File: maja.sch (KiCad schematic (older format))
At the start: 49 parts

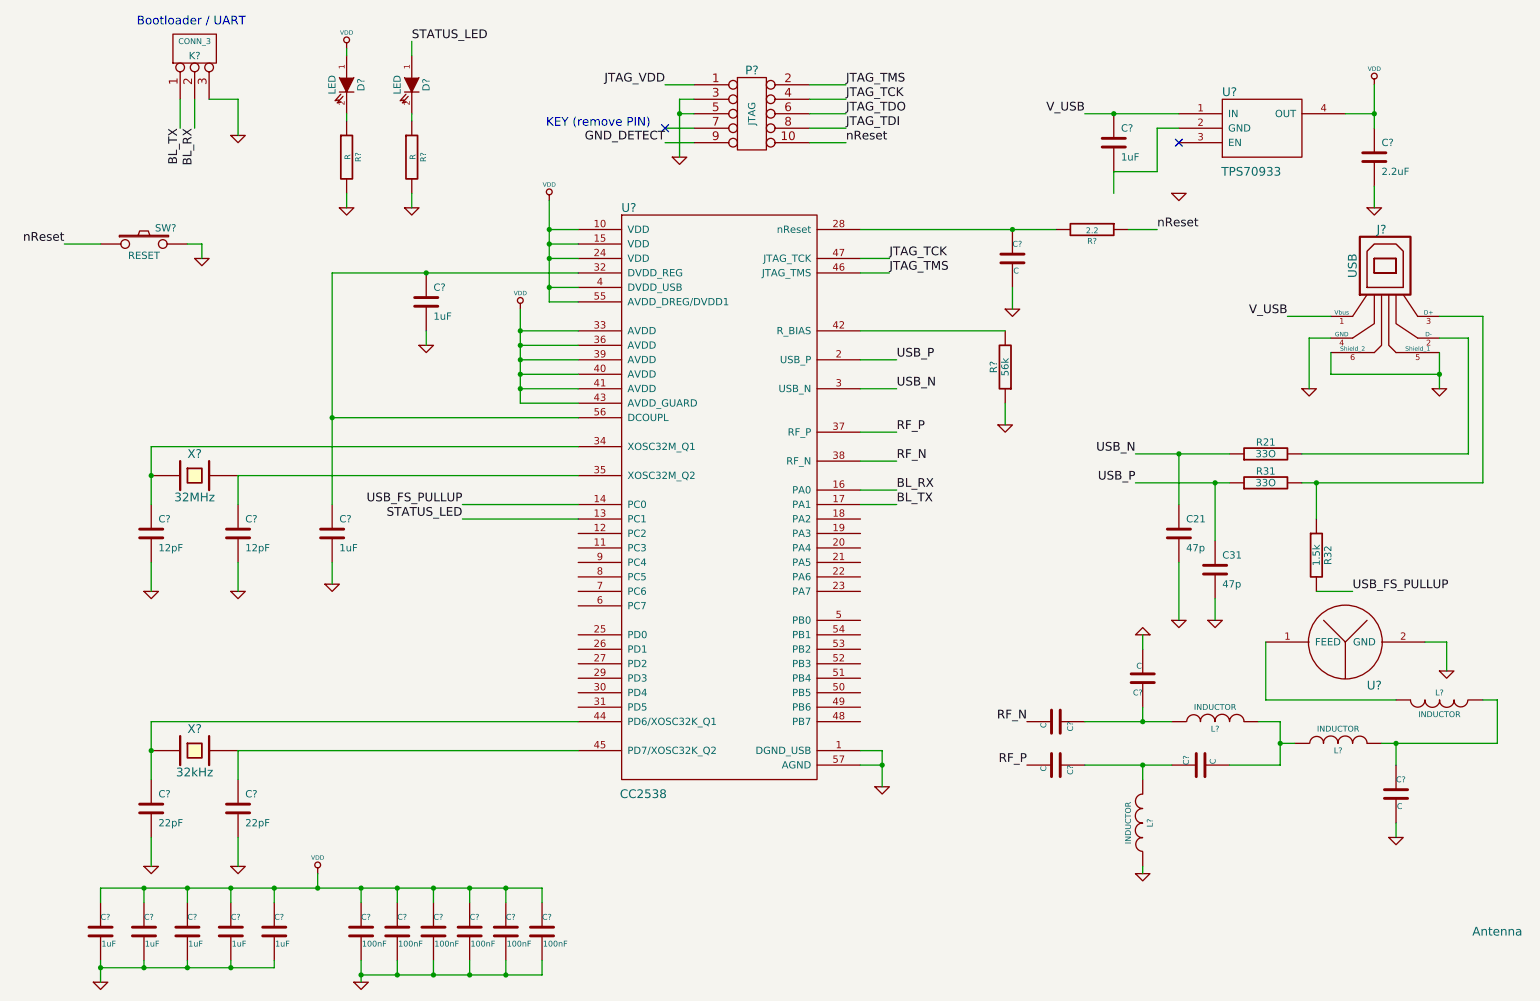
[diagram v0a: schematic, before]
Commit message: Started with basic PCB layout. Footprints must be checked again! I just choose one to be able to do a prelimary placement
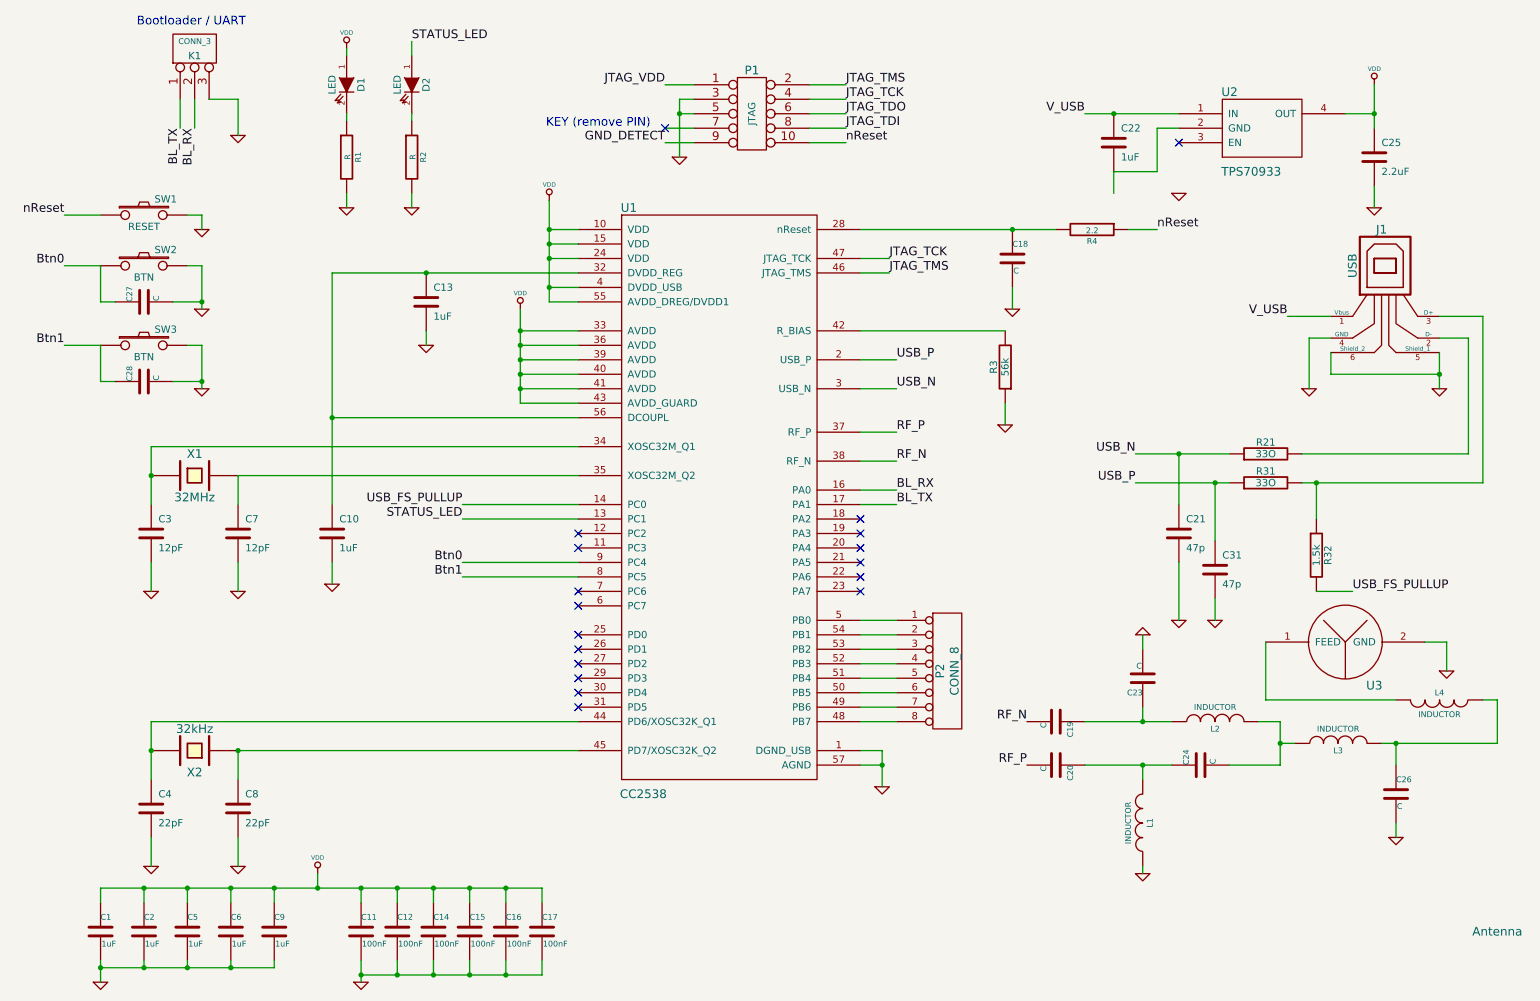
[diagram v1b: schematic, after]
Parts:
- added C27, C28: C, symbol C
- added P2: CONN_8, ~, symbol CONN_8
- added SW2, SW3: BTN, symbol SW_PUSH
- gave numbers to parts that had none: 44
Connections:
- net GND: now also C27.2, C28.2, SW2.2, SW3.2
- net at C4.1, U1.44 (PD6/XOSC32K_Q1): now also X2.2; no longer X2.1
- net at C8.1, U1.45 (PD7/XOSC32K_Q2): now also X2.1; no longer X2.2
- net at U1.48 (PB7): now also P2.8 (P8)
- net at U1.49 (PB6): now also P2.7 (P7)
- net at U1.5 (PB0): now also P2.1 (P1)
- net at U1.50 (PB5): now also P2.6 (P6)
- net at U1.51 (PB4): now also P2.5 (P5)
- net at U1.52 (PB3): now also P2.4 (P4)
- net at U1.53 (PB2): now also P2.3 (P3)
- net at U1.54 (PB1): now also P2.2 (P2)
- net Btn1: now reaches U1.8 (PC5)
- net Btn1: now also C28.1, SW3.1
- net Btn0: now reaches U1.9 (PC4)
- net Btn0: now also C27.1, SW2.1
- no-connect marks 2 -> 18
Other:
- moved on the sheet: SW1

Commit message: Started with routing, added two missing JTAG signals and corrected one library error
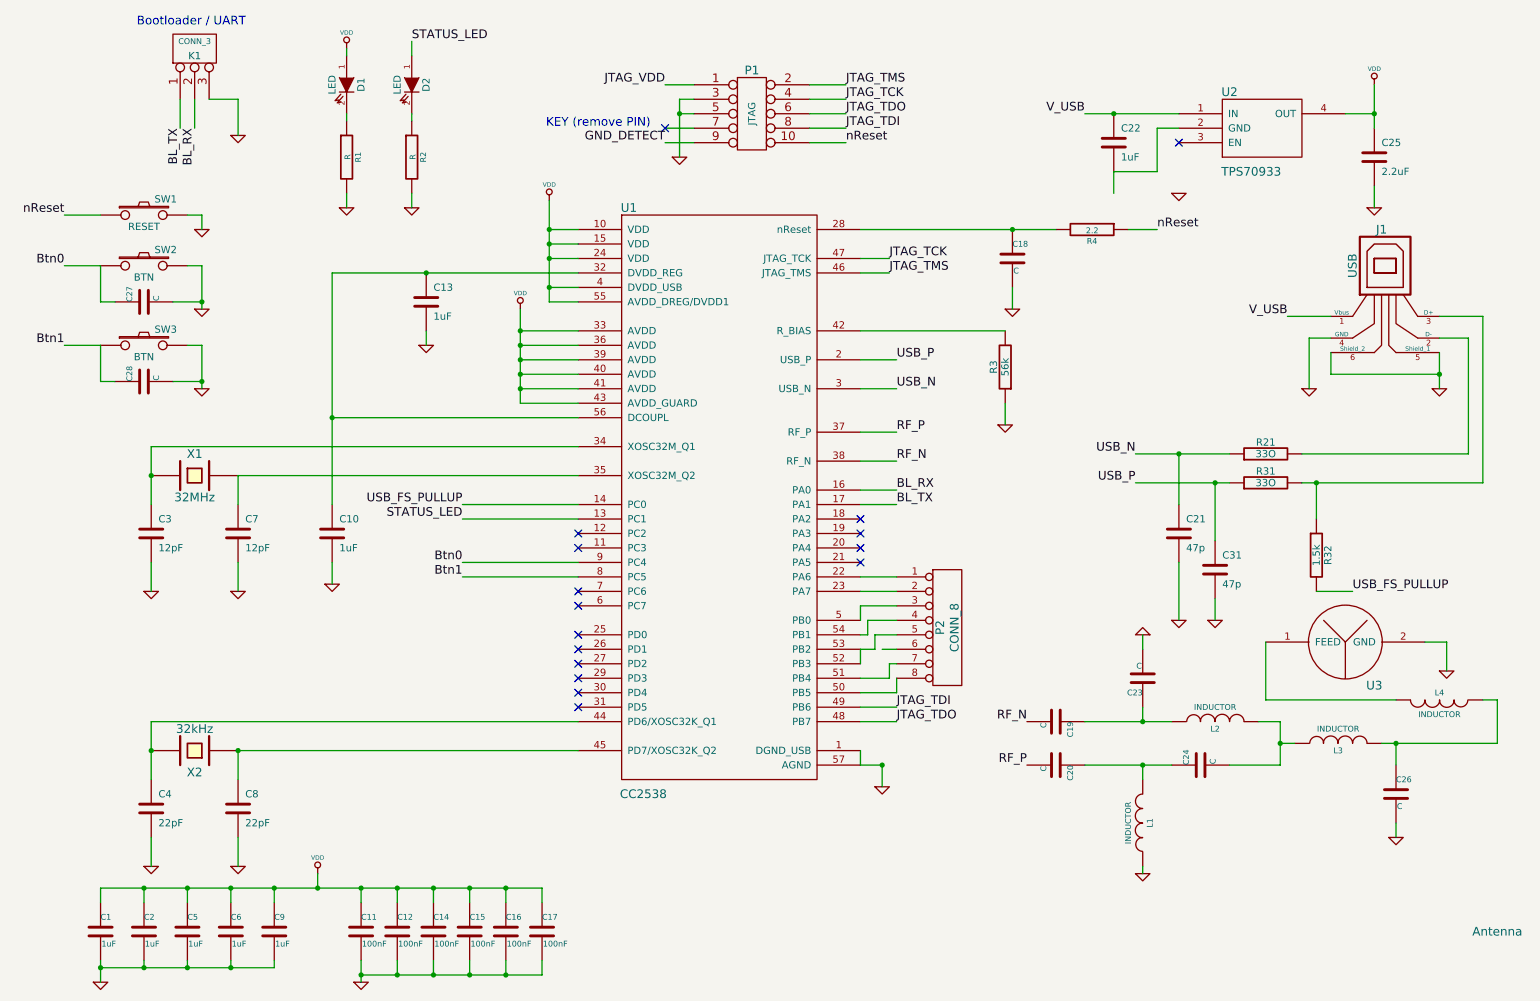
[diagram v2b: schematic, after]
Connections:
- net JTAG_TDI: now also U1.49 (PB6)
- net JTAG_TDO: now also U1.48 (PB7)
- net at U1.22 (PA6): now also P2.1 (P1)
- net at U1.23 (PA7): now also P2.2 (P2)
- net at P2.8 (P8): now also U1.50 (PB5); no longer U1.48 (PB7)
- net at P2.7 (P7): now also U1.51 (PB4); no longer U1.49 (PB6)
- net at U1.5 (PB0): now also P2.3 (P3); no longer P2.1 (P1)
- net at P2.6 (P6): no longer U1.50 (PB5)
- net at P2.5 (P5): now also U1.52 (PB3), U1.53 (PB2); no longer U1.51 (PB4)
- net at P2.4 (P4): now also U1.54 (PB1); no longer U1.52 (PB3)
- no-connect marks 18 -> 16
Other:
- moved on the sheet: P2
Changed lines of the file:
@@
 	0    -1   -1   0
-$EndComp
-$Comp
-L CC2538 U1
-U 1 1 531346AC
-P 5950 4950
-F 0 "U1" H 5050 8050 60  0000 C CNN
-F 1 "CC2538" H 5150 4000 60  0000 C CNN
-F 2 "" H 5950 4950 60  0001 C CNN
-F 3 "" H 5950 4950 60  0001 C CNN
-	1    5950 4950
-	1    0    0    -1
 $EndComp
 Text Label 1950 1300 3    60   ~ 0
@@
 	9750 2750 9900 2750
 Wire Wire Line
-	10650 2850 10650 3100
+	10650 2850 10650 3000
+Wire Wire Line
+	10650 3000 10650 3100
 Wire Wire Line
 	10650 2600 10950 2600
@@
 	10950 2600 10950 3750
 Wire Wire Line
-	10950 3750 9700 3750
+	10950 3750 9800 3750
+Wire Wire Line
+	9800 3750 9700 3750
 Wire Wire Line
 	4700 3900 3900 3900
@@
 	9100 4550 9100 4700
 Wire Wire Line
-	8550 3750 9200 3750
-Wire Wire Line
-	8550 3550 9200 3550
+	8550 3750 9100 3750
+Wire Wire Line
+	9100 3750 9200 3750
+Wire Wire Line
+	8550 3550 8850 3550
+Wire Wire Line
+	8850 3550 9200 3550
 Wire Wire Line
 	6650 2900 6900 2900
@@
 	2350 3700 4700 3700
 Wire Wire Line
-	1750 3500 1750 3900
+	1750 3500 1750 3700
+Wire Wire Line
+	1750 3700 1750 3900
 Connection ~ 1750 3700
 Wire Wire Line
@@
 	10200 1200 10000 1200
 Wire Wire Line
-	10200 1000 10200 1300
+	10200 1000 10200 1200
+Wire Wire Line
+	10200 1200 10200 1300
 Connection ~ 10200 1200
 Wire Wire Line
@@
 	8400 1600 8400 1750
 Wire Wire Line
-	8200 1200 8850 1200
+	8200 1200 8400 1200
+Wire Wire Line
+	8400 1200 8850 1200
 Connection ~ 8400 1200
 Wire Wire Line
-	3000 2300 4700 2300
-Wire Wire Line
-	3000 2300 3000 3900
+	3000 2300 3650 2300
+Wire Wire Line
+	3650 2300 4700 2300
+Wire Wire Line
+	3000 2300 3000 3300
+Wire Wire Line
+	3000 3300 3000 3900
 Connection ~ 3650 2300
 Wire Wire Line
@@
 	6650 3900 6900 3900
 Wire Wire Line
-	6650 5600 6800 5600
-Wire Wire Line
-	6800 5600 6800 5850
+	6650 5600 6650 5600
+Wire Wire Line
+	6650 5600 6650 5700
+Wire Wire Line
+	6800 5700 6800 5850
 Wire Wire Line
 	6650 5700 6800 5700
@@
 	7700 2550 7700 2400
 Wire Wire Line
-	6650 2000 8000 2000
+	6650 2000 7700 2000
+Wire Wire Line
+	7700 2000 8000 2000
 Connection ~ 7700 2000
 Wire Wire Line
@@
 	4500 2500 4700 2500
 Wire Wire Line
-	4500 1800 4500 2500
+	4500 1800 4500 2000
+Wire Wire Line
+	4500 2000 4500 2100
+Wire Wire Line
+	4500 2100 4500 2200
+Wire Wire Line
+	4500 2200 4500 2400
+Wire Wire Line
+	4500 2400 4500 2500
 Wire Wire Line
 	4700 2000 4500 2000
@@
 	4300 3200 4700 3200
 Wire Wire Line
-	4300 2550 4300 3200
+	4300 2550 4300 2700
+Wire Wire Line
+	4300 2700 4300 2800
+Wire Wire Line
+	4300 2800 4300 2900
+Wire Wire Line
+	4300 2900 4300 3000
+Wire Wire Line
+	4300 3000 4300 3100
+Wire Wire Line
+	4300 3100 4300 3200
 Wire Wire Line
 	4700 2700 4300 2700
@@
 	1400 6650 1400 6550
 Wire Wire Line
-	1400 6550 4450 6550
+	1400 6550 1700 6550
+Wire Wire Line
+	1700 6550 2000 6550
+Wire Wire Line
+	2000 6550 2300 6550
+Wire Wire Line
+	2300 6550 2600 6550
+Wire Wire Line
+	2600 6550 2900 6550
+Wire Wire Line
+	2900 6550 3200 6550
+Wire Wire Line
+	3200 6550 3450 6550
+Wire Wire Line
+	3450 6550 3700 6550
+Wire Wire Line
+	3700 6550 3950 6550
+Wire Wire Line
+	3950 6550 4200 6550
+Wire Wire Line
+	4200 6550 4450 6550
 Wire Wire Line
 	1700 6650 1700 6550
@@
 Connection ~ 2600 6550
 Wire Wire Line
-	1400 7050 1400 7200
-Wire Wire Line
-	1400 7100 2600 7100
+	1400 7050 1400 7100
+Wire Wire Line
+	1400 7100 1400 7200
+Wire Wire Line
+	1400 7100 1700 7100
+Wire Wire Line
+	1700 7100 2000 7100
+Wire Wire Line
+	2000 7100 2300 7100
+Wire Wire Line
+	2300 7100 2600 7100
 Wire Wire Line
 	2600 7100 2600 7050
@@
 	4450 7150 4450 7050
 Wire Wire Line
-	3200 7150 4450 7150
-Wire Wire Line
-	3200 7050 3200 7200
+	3200 7150 3450 7150
+Wire Wire Line
+	3450 7150 3700 7150
+Wire Wire Line
+	3700 7150 3950 7150
+Wire Wire Line
+	3950 7150 4200 7150
+Wire Wire Line
+	4200 7150 4450 7150
+Wire Wire Line
+	3200 7050 3200 7150
+Wire Wire Line
+	3200 7150 3200 7200
 Connection ~ 3200 7150
 Wire Wire Line
@@
 	5500 1100 5400 1100
 Wire Wire Line
-	5400 1100 5400 1500
+	5400 1100 5400 1200
+Wire Wire Line
+	5400 1200 5400 1500
 Wire Wire Line
 	5500 1200 5400 1200
@@
 	2350 5600 4700 5600
 Wire Wire Line
-	1750 5400 1750 5800
+	1750 5400 1750 5600
+Wire Wire Line
+	1750 5600 1750 5800
 Connection ~ 1750 5600
 Wire Wire Line
 	2350 6400 2350 6200
 Wire Wire Line
-	8200 5400 8800 5400
-Wire Wire Line
-	8200 5700 8800 5700
+	8200 5400 8600 5400
+Wire Wire Line
+	8600 5400 8800 5400
+Wire Wire Line
+	8200 5700 8600 5700
+Wire Wire Line
+	8600 5700 8800 5700
 Wire Wire Line
 	8600 5800 8600 5700
@@
 	9550 5700 9200 5700
 Wire Wire Line
-	9550 5400 9550 5700
+	9550 5400 9550 5550
+Wire Wire Line
+	9550 5550 9550 5700
 Wire Wire Line
 	9550 5550 9650 5550
@@
 Connection ~ 9550 5550
 Wire Wire Line
-	10250 5550 11050 5550
+	10250 5550 10350 5550
+Wire Wire Line
+	10350 5550 11050 5550
 Wire Wire Line
 	10350 5700 10350 5550
@@
 L CONN_8 P2
 U 1 1 53206D00
-P 7250 5050
-F 0 "P2" V 7200 5050 60  0000 C CNN
-F 1 "CONN_8" V 7300 5050 60  0000 C CNN
-F 2 "~" H 7250 5050 60  0000 C CNN
-F 3 "~" H 7250 5050 60  0000 C CNN
-	1    7250 5050
+P 7250 4750
+F 0 "P2" V 7200 4750 60  0000 C CNN
+F 1 "CONN_8" V 7300 4750 60  0000 C CNN
+F 2 "~" H 7250 4750 60  0000 C CNN
+F 3 "~" H 7250 4750 60  0000 C CNN
+	1    7250 4750
 	1    0    0    -1
 $EndComp
@@
 	2000 2250 2100 2250
 Wire Wire Line
-	2100 2250 2100 2550
+	2100 2250 2100 2500
+Wire Wire Line
+	2100 2500 2100 2550
 Wire Wire Line
 	1400 2250 1150 2250
@@
 $EndComp
 Wire Wire Line
-	2100 2800 2100 3100
+	2100 2800 2100 3050
+Wire Wire Line
+	2100 3050 2100 3100
 Wire Wire Line
 	2100 2800 2000 2800
@@
 Wire Wire Line
 	3900 4300 4700 4300
-Wire Wire Line
-	6650 4700 6900 4700
-Wire Wire Line
-	6650 4800 6900 4800
-Wire Wire Line
-	6650 4900 6900 4900
-Wire Wire Line
-	6650 5000 6900 5000
-Wire Wire Line
-	6650 5100 6900 5100
-Wire Wire Line
-	6650 5200 6900 5200
-Wire Wire Line
-	6650 5300 6900 5300
-Wire Wire Line
-	6650 5400 6900 5400
 $Comp
 L C C27
@@
 NoConn ~ 6650 4200
 NoConn ~ 6650 4300
-NoConn ~ 6650 4400
-NoConn ~ 6650 4500
 NoConn ~ 4700 4100
 NoConn ~ 4700 4200
@@
 NoConn ~ 4700 5300
 Connection ~ 2350 5600
+Wire Wire Line
+	6650 5400 6900 5400
+Wire Wire Line
+	6650 5300 6900 5300
+Text Label 6900 5300 0    60   ~ 0
+JTAG_TDI
+Text Label 6900 5400 0    60   ~ 0
+JTAG_TDO
+Wire Wire Line
+	6650 4400 6900 4400
+Wire Wire Line
+	6650 4500 6900 4500
+Wire Wire Line
+	6650 4700 6650 4600
+Wire Wire Line
+	6650 4600 6900 4600
+Wire Wire Line
+	6650 4800 6700 4800
+Wire Wire Line
+	6700 4800 6700 4700
+Wire Wire Line
+	6700 4700 6900 4700
+Wire Wire Line
+	6650 4900 6750 4900
+Wire Wire Line
+	6750 4900 6750 4800
+Wire Wire Line
+	6750 4800 6900 4800
+Wire Wire Line
+	6650 5000 6650 5000
+Wire Wire Line
+	6650 5000 6650 4900
+Wire Wire Line
+	6800 4900 6900 4900
+Wire Wire Line
+	6900 5000 6850 5000
+Wire Wire Line
+	6850 5000 6850 5100
+Wire Wire Line
+	6850 5100 6650 5100
+Wire Wire Line
+	6650 5200 6900 5200
+Wire Wire Line
+	6900 5200 6900 5100
+$Comp
+L CC2538 U1
+U 1 1 5326EB41
+P 5950 4950
+F 0 "U1" H 5050 8050 60  0000 C CNN
+F 1 "CC2538" H 5150 4000 60  0000 C CNN
+F 2 "" H 5950 4950 60  0000 C CNN
+F 3 "" H 5950 4950 60  0000 C CNN
+	1    5950 4950
+	1    0    0    -1
+$EndComp
 $EndSCHEMATC

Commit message: ...
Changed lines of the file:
@@
 	9750 2750 9900 2750
 Wire Wire Line
-	10650 2850 10650 3000
-Wire Wire Line
-	10650 3000 10650 3100
+	10650 2850 10650 3100
 Wire Wire Line
 	10650 2600 10950 2600
@@
 	10950 2600 10950 3750
 Wire Wire Line
-	10950 3750 9800 3750
-Wire Wire Line
-	9800 3750 9700 3750
+	10950 3750 9700 3750
 Wire Wire Line
 	4700 3900 3900 3900
@@
 	9100 4550 9100 4700
 Wire Wire Line
-	8550 3750 9100 3750
-Wire Wire Line
-	9100 3750 9200 3750
-Wire Wire Line
-	8550 3550 8850 3550
-Wire Wire Line
-	8850 3550 9200 3550
+	8550 3750 9200 3750
+Wire Wire Line
+	8550 3550 9200 3550
 Wire Wire Line
 	6650 2900 6900 2900
@@
 	2350 3700 4700 3700
 Wire Wire Line
-	1750 3500 1750 3700
-Wire Wire Line
-	1750 3700 1750 3900
+	1750 3500 1750 3900
 Connection ~ 1750 3700
 Wire Wire Line
@@
 	10200 1200 10000 1200
 Wire Wire Line
-	10200 1000 10200 1200
-Wire Wire Line
-	10200 1200 10200 1300
+	10200 1000 10200 1300
 Connection ~ 10200 1200
 Wire Wire Line
@@
 	8400 1600 8400 1750
 Wire Wire Line
-	8200 1200 8400 1200
-Wire Wire Line
-	8400 1200 8850 1200
+	8200 1200 8850 1200
 Connection ~ 8400 1200
 Wire Wire Line
-	3000 2300 3650 2300
-Wire Wire Line
-	3650 2300 4700 2300
-Wire Wire Line
-	3000 2300 3000 3300
-Wire Wire Line
-	3000 3300 3000 3900
+	3000 2300 4700 2300
+Wire Wire Line
+	3000 2300 3000 3900
 Connection ~ 3650 2300
 Wire Wire Line
@@
 	7700 2550 7700 2400
 Wire Wire Line
-	6650 2000 7700 2000
-Wire Wire Line
-	7700 2000 8000 2000
+	6650 2000 8000 2000
 Connection ~ 7700 2000
 Wire Wire Line
@@
 	4500 2500 4700 2500
 Wire Wire Line
-	4500 1800 4500 2000
-Wire Wire Line
-	4500 2000 4500 2100
-Wire Wire Line
-	4500 2100 4500 2200
-Wire Wire Line
-	4500 2200 4500 2400
-Wire Wire Line
-	4500 2400 4500 2500
+	4500 1800 4500 2500
 Wire Wire Line
 	4700 2000 4500 2000
@@
 	4300 3200 4700 3200
 Wire Wire Line
-	4300 2550 4300 2700
-Wire Wire Line
-	4300 2700 4300 2800
-Wire Wire Line
-	4300 2800 4300 2900
-Wire Wire Line
-	4300 2900 4300 3000
-Wire Wire Line
-	4300 3000 4300 3100
-Wire Wire Line
-	4300 3100 4300 3200
+	4300 2550 4300 3200
 Wire Wire Line
 	4700 2700 4300 2700
@@
 	1400 6650 1400 6550
 Wire Wire Line
-	1400 6550 1700 6550
-Wire Wire Line
-	1700 6550 2000 6550
-Wire Wire Line
-	2000 6550 2300 6550
-Wire Wire Line
-	2300 6550 2600 6550
-Wire Wire Line
-	2600 6550 2900 6550
-Wire Wire Line
-	2900 6550 3200 6550
-Wire Wire Line
-	3200 6550 3450 6550
-Wire Wire Line
-	3450 6550 3700 6550
-Wire Wire Line
-	3700 6550 3950 6550
-Wire Wire Line
-	3950 6550 4200 6550
-Wire Wire Line
-	4200 6550 4450 6550
+	1400 6550 4450 6550
 Wire Wire Line
 	1700 6650 1700 6550
@@
 Connection ~ 2600 6550
 Wire Wire Line
-	1400 7050 1400 7100
-Wire Wire Line
-	1400 7100 1400 7200
-Wire Wire Line
-	1400 7100 1700 7100
-Wire Wire Line
-	1700 7100 2000 7100
-Wire Wire Line
-	2000 7100 2300 7100
-Wire Wire Line
-	2300 7100 2600 7100
+	1400 7050 1400 7200
+Wire Wire Line
+	1400 7100 2600 7100
 Wire Wire Line
 	2600 7100 2600 7050
@@
 	4450 7150 4450 7050
 Wire Wire Line
-	3200 7150 3450 7150
-Wire Wire Line
-	3450 7150 3700 7150
-Wire Wire Line
-	3700 7150 3950 7150
-Wire Wire Line
-	3950 7150 4200 7150
-Wire Wire Line
-	4200 7150 4450 7150
-Wire Wire Line
-	3200 7050 3200 7150
-Wire Wire Line
-	3200 7150 3200 7200
+	3200 7150 4450 7150
+Wire Wire Line
+	3200 7050 3200 7200
 Connection ~ 3200 7150
 Wire Wire Line
@@
 	5500 1100 5400 1100
 Wire Wire Line
-	5400 1100 5400 1200
-Wire Wire Line
-	5400 1200 5400 1500
+	5400 1100 5400 1500
 Wire Wire Line
 	5500 1200 5400 1200
@@
 	2350 5600 4700 5600
 Wire Wire Line
-	1750 5400 1750 5600
-Wire Wire Line
-	1750 5600 1750 5800
+	1750 5400 1750 5800
 Connection ~ 1750 5600
 Wire Wire Line
 	2350 6400 2350 6200
 Wire Wire Line
-	8200 5400 8600 5400
-Wire Wire Line
-	8600 5400 8800 5400
-Wire Wire Line
-	8200 5700 8600 5700
-Wire Wire Line
-	8600 5700 8800 5700
+	8200 5400 8800 5400
+Wire Wire Line
+	8200 5700 8800 5700
 Wire Wire Line
 	8600 5800 8600 5700
@@
 	9550 5700 9200 5700
 Wire Wire Line
-	9550 5400 9550 5550
-Wire Wire Line
-	9550 5550 9550 5700
+	9550 5400 9550 5700
 Wire Wire Line
 	9550 5550 9650 5550
@@
 Connection ~ 9550 5550
 Wire Wire Line
-	10250 5550 10350 5550
-Wire Wire Line
-	10350 5550 11050 5550
+	10250 5550 11050 5550
 Wire Wire Line
 	10350 5700 10350 5550
@@
 	2000 2250 2100 2250
 Wire Wire Line
-	2100 2250 2100 2500
-Wire Wire Line
-	2100 2500 2100 2550
+	2100 2250 2100 2550
 Wire Wire Line
 	1400 2250 1150 2250
@@
 $EndComp
 Wire Wire Line
-	2100 2800 2100 3050
-Wire Wire Line
-	2100 3050 2100 3100
+	2100 2800 2100 3100
 Wire Wire Line
 	2100 2800 2000 2800
